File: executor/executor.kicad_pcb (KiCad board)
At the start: 2 copper layers, 0 parts

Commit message: [New] complete executor PCB layout
Signed-off-by: Homalozoa <nx.tardis@gmail.com>
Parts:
- added C1: 10uF, 20%, 50V, Capacitor_SMD:C_0805_2012Metric, F.Cu at (72.5, 69.2)
- added C10: 10uF, 10%, 50V, Capacitor_SMD:C_0402_1005Metric, B.Cu at (59.1, 67.6)
- added C11: 10uF, 20%, 50V, Capacitor_SMD:C_0805_2012Metric, F.Cu at (69.1, 83.2)
- added C12: 15pF, 5%, 50V, Capacitor_SMD:C_0402_1005Metric, B.Cu at (58.0, 69.5)
- added C13: 10uF, 20%, 50V, Capacitor_SMD:C_0805_2012Metric, F.Cu at (69.1, 81.2)
- added C14: 10uF, 20%, 50V, Capacitor_SMD:C_0805_2012Metric, F.Cu at (69.1, 79.2)
- added C15: 10uF, 20%, 50V, Capacitor_SMD:C_0805_2012Metric, F.Cu at (69.1, 77.2)
- added C16: 100nF, 10%, 50V, Capacitor_SMD:C_0402_1005Metric, B.Cu at (56.9, 67.6)
- added C17: 1uF, 10%, 50V, Capacitor_SMD:C_0402_1005Metric, F.Cu at (71.4, 45.5)
- added C18: 10uF, 20%, 50V, Capacitor_SMD:C_0805_2012Metric, F.Cu at (69.0, 75.2)
- added C19: 10uF, 20%, 50V, Capacitor_SMD:C_0805_2012Metric, F.Cu at (69.1, 73.2)
- added C2: 10uF, 20%, 50V, Capacitor_SMD:C_0805_2012Metric, F.Cu at (72.5, 71.2)
- added C20: 10uF, 20%, 50V, Capacitor_SMD:C_0805_2012Metric, F.Cu at (69.1, 71.2)
- added C21: 10uF, 20%, 50V, Capacitor_SMD:C_0805_2012Metric, F.Cu at (69.1, 69.2)
- added C22: 47uF, 10% 50V, Capacitor_SMD:CP_Elec_8x6.2, B.Cu at (70.9, 82.0)
- added C23: 100nF, 10%, 50V, Capacitor_SMD:C_0402_1005Metric, B.Cu at (67.0, 67.8)
- added C24: 100nF, 10%, 50V, Capacitor_SMD:C_0402_1005Metric, B.Cu at (70.8, 70.9)
- added C25: 1uF, 10%, 50V, Capacitor_SMD:C_0402_1005Metric, F.Cu at (79.9, 45.5)
- added C26: 4.7uF, 20%, 50V, Capacitor_SMD:C_0603_1608Metric, B.Cu at (71.1, 75.1)
- added C27: 100nF, 10%, 10V, Capacitor_SMD:C_0402_1005Metric, F.Cu at (94.2, 72.6)
- added C28: 4.7uF, 20%, 50V, Capacitor_SMD:C_0603_1608Metric, B.Cu at (72.7, 75.1)
- added C29: 1uF, 10%, 50V, Capacitor_SMD:C_0402_1005Metric, F.Cu at (87.6, 37.3)
- added C3: 10uF, 20%, 50V, Capacitor_SMD:C_0805_2012Metric, F.Cu at (72.5, 73.2)
- added C30: 100nF, 10%, 50V, Capacitor_SMD:C_0402_1005Metric, B.Cu at (72.8, 70.9)
- added C31: 4.7uF, 20%, 50V, Capacitor_SMD:C_0603_1608Metric, B.Cu at (61.6, 57.0)
- added C32: 1nF, 10%, 50V, Capacitor_SMD:C_0402_1005Metric, F.Cu at (48.1, 56.5)
- added C33: 100nF, 10%, 10V, Capacitor_SMD:C_0402_1005Metric, F.Cu at (87.6, 71.1)
- added C34: 4.7uF, 20%, 50V, Capacitor_SMD:C_0603_1608Metric, B.Cu at (61.6, 55.4)
- added C35: 1nF, 10%, 50V, Capacitor_SMD:C_0402_1005Metric, F.Cu at (48.1, 57.5)
- added C36: 100nF, 10%, 50V, Capacitor_SMD:C_0402_1005Metric, F.Cu at (48.1, 55.4)
- added C37: 1uF, 10%, 50V, Capacitor_SMD:C_0402_1005Metric, F.Cu at (54.3, 52.3)
- added C38: 10pF, 10%, 10V, Capacitor_SMD:C_0402_1005Metric, F.Cu at (82.8, 66.1)
- added C39: 100nF, 10%, 10V, Capacitor_SMD:C_0402_1005Metric, B.Cu at (87.3, 67.1)
- added C4: 10uF, 20%, 50V, Capacitor_SMD:C_0805_2012Metric, F.Cu at (72.5, 75.2)
- added C40: 10uF, 10%, 10V, Capacitor_SMD:C_0402_1005Metric, F.Cu at (86.1, 71.8)
- added C41: 100nF, 10%, 10V, Capacitor_SMD:C_0402_1005Metric, B.Cu at (96.0, 53.5)
- added C42: 10pF, 10%, 10V, Capacitor_SMD:C_0402_1005Metric, F.Cu at (86.2, 69.7)
- added C43: 100nF, 10%, 10V, Capacitor_SMD:C_0402_1005Metric, F.Cu at (85.4, 72.5)
- added C44: 100nF, 10%, 10V, Capacitor_SMD:C_0402_1005Metric, B.Cu at (93.2, 56.3)
- added C45: 10uF, 10%, 10V, Capacitor_SMD:C_0402_1005Metric, B.Cu at (88.9, 69.7)
- added C46: 100nF, 10%, 10V, Capacitor_SMD:C_0402_1005Metric, B.Cu at (89.6, 69.0)
- added C47: 4.7uF, 10%, 10V, Capacitor_SMD:C_0402_1005Metric, B.Cu at (94.6, 54.9)
- added C48: 1uF, 10%, 10V, Capacitor_SMD:C_0402_1005Metric, F.Cu at (58.9, 59.4)
- added C49: 47nF, 10%, 50V, Capacitor_SMD:C_0402_1005Metric, F.Cu at (56.2, 52.3)
- added C5: 10uF, 20%, 50V, Capacitor_SMD:C_0805_2012Metric, F.Cu at (72.5, 77.2)
- added C50: 1uF, 10%, 10V, Capacitor_SMD:C_0402_1005Metric, B.Cu at (93.9, 55.6)
- added C51: 100nF, 10%, 10V, Capacitor_SMD:C_0402_1005Metric, B.Cu at (95.3, 54.2)
- added C52: 100nF, 10%, 10V, Capacitor_SMD:C_0402_1005Metric, F.Cu at (61.0, 58.3)
- added C53: 10pF, 10%, 50V, Capacitor_SMD:C_0402_1005Metric, B.Cu at (81.0, 66.3)
- added C54: 10nF, 10%, 50V, Capacitor_SMD:C_0402_1005Metric, B.Cu at (75.4, 73.2)
- added C55: 10pF, 10%, 50V, Capacitor_SMD:C_0402_1005Metric, B.Cu at (75.9, 65.9)
- added C56: 10nF, 10%, 10V, Capacitor_SMD:C_0402_1005Metric, F.Cu at (72.1, 65.1)
- added C57: 2.2uF, 10%, 10V, Capacitor_SMD:C_0402_1005Metric, F.Cu at (72.1, 64.1)
- added C58: 100nnF, 10%, 10V, Capacitor_SMD:C_0402_1005Metric, F.Cu at (72.1, 63.1)
- added C59: 300nF, 10%, 50V, Capacitor_SMD:C_0402_1005Metric, B.Cu at (75.9, 68.2)
- added C6: 10uF, 10%, 50V, Capacitor_SMD:C_0402_1005Metric, B.Cu at (58.0, 67.6)
- added C60: 100pF, 10%, 10V, Capacitor_SMD:C_0402_1005Metric, B.Cu at (81.2, 74.9)
- added C61: 100nF, 10%, 10V, Capacitor_SMD:C_0402_1005Metric, B.Cu at (69.5, 59.4)
- added C62: 100pF, 10%, 10V, Capacitor_SMD:C_0402_1005Metric, B.Cu at (76.0, 75.5)
- added C63: 1uF, 10%, 10V, Capacitor_SMD:C_0402_1005Metric, B.Cu at (70.5, 59.4)
- added C64: 100nF, 10%, 50V, Capacitor_SMD:C_0402_1005Metric, B.Cu at (74.8, 70.9)
- added C65: 10uF, 10%, 50V, Capacitor_SMD:C_0402_1005Metric, B.Cu at (75.8, 70.9)
- added C66: 10uF, 10%, 50V, Capacitor_SMD:C_0402_1005Metric, B.Cu at (74.3, 69.5)
- added C7: 10uF, 20%, 50V, Capacitor_SMD:C_0805_2012Metric, F.Cu at (72.5, 79.2)
- added C8: 10uF, 20%, 50V, Capacitor_SMD:C_0805_2012Metric, F.Cu at (72.5, 81.2)
- added C9: 10uF, 20%, 50V, Capacitor_SMD:C_0805_2012Metric, F.Cu at (72.5, 83.2)
- added D1: 5V, Diode_SMD:D_SOD-923, B.Cu at (55.8, 67.7)
- added D2: BAV99, Package_TO_SOT_SMD:SOT-23, B.Cu at (61.5, 78.6)
- added D3: ESD56161D30, Rolling_Custom:DFN2x2-3L, B.Cu at (68.8, 74.4)
- added D4: BAV99, Package_TO_SOT_SMD:SOT-23, B.Cu at (50.1, 64.4)
- added D5: BAV99, Package_TO_SOT_SMD:SOT-23, B.Cu at (53.8, 64.4)
- added D6: BAV99, Package_TO_SOT_SMD:SOT-23, B.Cu at (57.6, 64.4)
- added D7: Blue, LED_SMD:LED_0402_1005Metric, F.Cu at (97.6, 73.3)
- added D8: 12V, Diode_SMD:D_SOD-323, B.Cu at (79.6, 75.0)
- added D9: 12V, Diode_SMD:D_SOD-323, B.Cu at (77.6, 75.0)
- added J1: XT30PW(2+2), Rolling_Custom:XT30PW(2+2), F.Cu at (83.3, 82.8)
- added L1: 10uH, Inductor_SMD:L_Coilcraft_XxL4040, B.Cu at (62.2, 68.2)
- added L2: 20R, Resistor_SMD:R_0402_1005Metric, B.Cu at (88.1, 71.2)
- added NT1: NetTie, NetTie:NetTie-2_SMD_Pad0.5mm, F.Cu at (74.0, 66.3)
- added Q1: WNM6006, Rolling_Custom:PDFN5X6-8L, F.Cu at (67.8, 39.9)
- added Q2: WNM6006, Rolling_Custom:PDFN5X6-8L, F.Cu at (67.8, 51.2)
- added Q3: WNM6006, Rolling_Custom:PDFN5X6-8L, F.Cu at (75.8, 39.9)
- added Q4: WNM6006, Rolling_Custom:PDFN5X6-8L, F.Cu at (75.8, 51.2)
- added Q5: WNM6006, Rolling_Custom:PDFN5X6-8L, F.Cu at (83.2, 39.9)
- added Q6: WNM6006, Rolling_Custom:PDFN5X6-8L, F.Cu at (83.2, 51.2)
- added R1: 0, Resistor_SMD:R_0402_1005Metric, F.Cu at (63.9, 49.2)
- added R10: 100k, 5%, Resistor_SMD:R_0402_1005Metric, B.Cu at (71.3, 72.9)
- added R11: 100k, 5%, Resistor_SMD:R_0402_1005Metric, B.Cu at (71.8, 70.9)
- added R12: 0, Resistor_SMD:R_0402_1005Metric, F.Cu at (79.7, 37.4)
- added R13: 0, Resistor_SMD:R_0402_1005Metric, F.Cu at (79.7, 48.6)
- added R14: 10k, 5%, Resistor_SMD:R_0402_1005Metric, F.Cu at (93.4, 71.8)
- added R15: 10k, 5%, Resistor_SMD:R_0402_1005Metric, F.Cu at (92.6, 71.0)
- added R16: 0.001R, Resistor_SMD:R_1206_3216Metric, F.Cu at (55.4, 46.9)
- added R17: 10k, 5%, Resistor_SMD:R_0402_1005Metric, F.Cu at (86.9, 70.4)
- added R18: 10k, 5%, Resistor_SMD:R_0402_1005Metric, B.Cu at (88.1, 67.9)
- added R19: 0, Resistor_SMD:R_0402_1005Metric, B.Cu at (87.3, 70.4)
- added R2: 0, Resistor_SMD:R_0402_1005Metric, F.Cu at (63.9, 37.4)
- added R20: 10k, 5%, Resistor_SMD:R_0402_1005Metric, F.Cu at (61.0, 59.4)
- added R21: 100R, 5%, Resistor_SMD:R_0402_1005Metric, F.Cu at (61.0, 60.5)
- added R22: 100R, 5%, Resistor_SMD:R_0402_1005Metric, F.Cu at (61.0, 61.5)
- added R23: 100R, 5%, Resistor_SMD:R_0402_1005Metric, F.Cu at (61.0, 62.5)
- added R27: 10k, 5%, Resistor_SMD:R_0402_1005Metric, F.Cu at (84.8, 59.5)
- added R28: 0R, 5%, Resistor_SMD:R_0402_1005Metric, B.Cu at (96.3, 59.1)
- added R29: 0R, 5%, Resistor_SMD:R_0402_1005Metric, B.Cu at (95.6, 58.4)
- added R3: 150k, 5%, Resistor_SMD:R_0402_1005Metric, B.Cu at (59.1, 69.5)
- added R30: 0R, 5%, Resistor_SMD:R_0402_1005Metric, B.Cu at (94.9, 57.7)
- added R31: 100R, 5%, Resistor_SMD:R_0402_1005Metric, B.Cu at (65.6, 79.8)
- added R32: 33k, Resistor_SMD:R_0402_1005Metric, B.Cu at (75.4, 74.1)
- added R33: 10k, 5%, Resistor_SMD:R_0402_1005Metric, F.Cu at (96.9, 72.6)
- added R34: 3k, Resistor_SMD:R_0402_1005Metric, B.Cu at (73.8, 70.9)
- added R36: 2.2k, 5%, Resistor_SMD:R_0402_1005Metric, F.Cu at (74.2, 57.6)
- added R37: 2.2k, 5%, Resistor_SMD:R_0402_1005Metric, F.Cu at (75.8, 57.6)
- added R38: 120R, Resistor_SMD:R_0402_1005Metric, B.Cu at (86.2, 76.2)
- added R4: 47k, 1%, Resistor_SMD:R_0402_1005Metric, B.Cu at (69.8, 70.9)
- added R5: 150k, 5%, Resistor_SMD:R_0402_1005Metric, B.Cu at (64.5, 81.8)
- added R6: 10k, 5%, Resistor_SMD:R_0402_1005Metric, B.Cu at (64.5, 79.8)
- added R7: 0, Resistor_SMD:R_0402_1005Metric, F.Cu at (72.0, 37.3)
- added R8: 0, Resistor_SMD:R_0402_1005Metric, F.Cu at (71.9, 48.6)
- added R9: 0.001R, Resistor_SMD:R_1206_3216Metric, F.Cu at (55.4, 49.2)
- added TP1: 3V3, TestPoint:TestPoint_Pad_D2.0mm, F.Cu at (50.6, 69.2)
- added TP10: C, TestPoint:TestPoint_Plated_Hole_D2.0mm, F.Cu at (83.4, 45.6)
- added TP13: NTC+, TestPoint:TestPoint_Loop_D1.80mm_Drill1.0mm_Beaded, F.Cu at (97.3, 47.2)
- added TP14: NTC-, TestPoint:TestPoint_Loop_D1.80mm_Drill1.0mm_Beaded, F.Cu at (99.7, 50.6)
- added TP4: SWDIO, TestPoint:TestPoint_Pad_D1.5mm, F.Cu at (102.1, 56.6)
- added TP5: SWCLK, TestPoint:TestPoint_Pad_D1.5mm, F.Cu at (101.0, 53.9)
- added TP7: A, TestPoint:TestPoint_Plated_Hole_D2.0mm, F.Cu at (68.0, 45.6)
- added TP8: B, TestPoint:TestPoint_Plated_Hole_D2.0mm, F.Cu at (76.0, 45.6)
- added U1: WD1601E, Package_TO_SOT_SMD:SOT-23-6, B.Cu at (67.0, 70.3)
- added U2: DRV8323SRTAT, Rolling_Custom:WQFN40, F.Cu at (54.1, 57.9)
- added U3: GD32F303RETx, Package_QFP:LQFP-64_10x10mm_P0.5mm, F.Cu at (92.0, 62.9)
- added U4: TCAN4550RGYRQ1, Rolling_Custom:VQFN20, B.Cu at (78.6, 70.5)
- added U5: AS5047P-ATSM, Package_SO:TSSOP-14_4.4x5mm_P0.65mm, B.Cu at (75.0, 60.0)
- added U6: QMA7981, Package_LGA:LGA-12_2x2mm_P0.5mm, F.Cu at (75.0, 60.0)
- added Y1: 8M, Oscillator:Oscillator_SMD_EuroQuartz_XO32-4Pin_3.2x2.5mm, F.Cu at (84.6, 67.8)
- added Y2: 40M, Oscillator:Oscillator_SMD_EuroQuartz_XO32-4Pin_3.2x2.5mm, B.Cu at (78.4, 66.2)
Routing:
- net GND: track 0.00 -> 240.9 mm, vias 0 -> 17
- net +3V3: track 0.00 -> 223.9 mm, vias 0 -> 14
- net VM: track 0.00 -> 170.9 mm, vias 0 -> 8
- net IAN: track 0.00 -> 170.4 mm, vias 0 -> 10
- net C: track 0.00 -> 77.6 mm, vias 0 -> 2
- net ICP: track 0.00 -> 69.6 mm, vias 0 -> 4
- net DRV_EN: track 0.00 -> 62.9 mm, vias 0 -> 4
- net IBP: track 0.00 -> 59.1 mm, vias 0 -> 4
- net DRV_SCK: track 0.00 -> 53.7 mm, vias 0 -> 2
- net DRV_SCS: track 0.00 -> 53.4 mm, vias 0 -> 2
- net B: track 0.00 -> 53.2 mm, vias 0 -> 3
- net DRV_SDO: track 0.00 -> 52.2 mm, vias 0 -> 2
- net DRV_SDI: track 0.00 -> 51.9 mm, vias 0 -> 2
- net ISENSE_A: track 0.00 -> 50.8 mm, vias 0 -> 2
- net PWM_A: track 0.00 -> 44.7 mm, vias 0 -> 2
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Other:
- board outline added: 58 x 58 mm
- copper layers 2 -> 4

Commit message: [New] Complete executor ver 0.1
Signed-off-by: Homalozoa <nx.tardis@gmail.com>
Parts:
- removed R16: 0.001R, Resistor_SMD:R_1206_3216Metric
- C10, C12, C16, C31, C34, C53, C54, C55, C59, C6, C60, C62, C64, C65, C66, D1, D4, D6, D8, D9, R3, R32, R34, R38, R4, R5, R6, U4, Y2: moved to F.Cu
- C17, C25, C29, C56, C57, C58, NT1, Q1, Q2, Q3, Q4, Q5, Q6, R1, R12, R13, R2, R7, R8, R9, TP10, TP7, TP8: moved to B.Cu
- moved TP14 51.8 mm to (53.9, 74.9)
- moved TP13 51.8 mm to (51.5, 71.4)
- moved TP4 50.3 mm to (53.2, 44.9), turned to 135 degrees
- moved TP5 50.2 mm to (51.4, 46.7), turned to 135 degrees
- moved Q1 41.1 mm to (97.5, 68.3), turned to 0 degrees
- moved R2 40.6 mm to (94.1, 64.6), turned to 0 degrees
- moved C11 38.6 mm to (82.2, 46.9), turned to 0 degrees
- moved D7 37.0 mm to (61.9, 82.9), turned to -135 degrees
- moved C27 36.5 mm to (58.1, 67.2)
- moved C45 35.5 mm to (53.7, 65.1)
- moved R17 35.5 mm to (51.7, 65.8)
- moved U3 35.5 mm to (56.8, 58.3)
- moved C33 35.5 mm to (52.4, 66.5)
- moved C39 35.5 mm to (52.1, 62.5)
- moved C46 35.5 mm to (54.4, 64.4)
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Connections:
- net IAN renamed GNDA
- net VM renamed +24V
- R29 pad 2: PWM_C -> PWM_B
- R30 pad 2: PWM_B -> PWM_C
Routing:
- net GND: track 240.9 -> 285.5 mm, vias 17 -> 10
- net CAN_L: track 19.1 -> 60.2 mm, vias 0 -> 2
- net A: track 44.5 -> 85.2 mm
- net ECD_MOSI: track 10.9 -> 47.5 mm, vias 1 -> 2
- net ECD_MISO: track 11.2 -> 44.6 mm, vias 1 -> 2
- net CAN_H: track 22.1 -> 54.7 mm, vias 0 -> 2
- net ICP: track 69.6 -> 37.8 mm, vias 4 -> 3
- net ECD_SCK: track 11.6 -> 41.2 mm, vias 1 -> 2
- net +24V: track 170.9 -> 200.2 mm, vias 8 -> 6
- net Net-(R31-Pad1): track 36.3 -> 7.32 mm, vias 2 -> 1
- net TCAN_SDO: track 33.0 -> 5.13 mm, vias 3 -> 0
- net TEMP_MOTOR: track 38.3 -> 10.6 mm, vias 2 -> 0
- net VGL_A: track 19.6 -> 46.4 mm
- net TCAN_SDI: track 31.8 -> 5.01 mm, vias 3 -> 2
- net VGH_A: track 21.8 -> 48.5 mm, vias 2 -> 3
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- added copper zone on In2.Cu, net +24V
- added copper zone on In1.Cu, net +3V3
- added copper zone on B.Cu, net GND
- added copper zone on F.Cu, net GND
- added copper zone on B.Cu, net GNDA
- added copper zone on F.Cu, net GNDA

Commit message: [New] Add prj cerebellum & limbic_cm4 & limbic_x3m
Signed-off-by: Homalozoa <nx.tardis@gmail.com>
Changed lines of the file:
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@@
   (gr_arc locked (start 98.276504 42.702475) (mid 103.997113 60) (end 98.276504 77.297525) (layer "Edge.Cuts") (width 0.15))
   (gr_arc locked (start 57.702475 83.276504) (mid 56.895935 81.638704) (end 57.755316 80.028002) (layer "Edge.Cuts") (width 0.15))
-  (gr_arc locked (start 51.723495 42.702475) (mid 53.361295 41.895935) (end 54.971998 42.755316) (layer "Edge.Cuts") (width 0.15))
+  (gr_arc locked (start 51.723495 42.702475) (mid 53.361295 41.895936) (end 54.971998 42.755316) (layer "Edge.Cuts") (width 0.15))
   (gr_arc locked (start 92.297526 83.276504) (mid 75.000001 88.997113) (end 57.702475 83.276504) (layer "Edge.Cuts") (width 0.15))
   (gr_arc locked (start 57.702474 36.723496) (mid 75 31.002886) (end 92.297525 36.723496) (layer "Edge.Cuts") (width 0.15))
@@
   (segment (start 86 56.485) (end 86 48.085) (width 0.254) (layer "In1.Cu") (net 37))
   (segment (start 86.4 56.885) (end 86 56.485) (width 0.254) (layer "In1.Cu") (net 37))
-  (segment (start 67.952957 37.288589) (end 74.584109 37.288589) (width 0.254) (layer "In2.Cu") (net 37))
   (segment (start 67.4 37.841546) (end 67.952957 37.288589) (width 0.254) (layer "In2.Cu") (net 37))
   (segment (start 85.38052 48.085) (end 86 48.085) (width 0.254) (layer "In2.Cu") (net 37))
   (segment (start 74.584109 37.288589) (end 85.38052 48.085) (width 0.254) (layer "In2.Cu") (net 37))
   (segment (start 67.4 38.885) (end 67.4 37.841546) (width 0.254) (layer "In2.Cu") (net 37))
+  (segment (start 67.952957 37.288589) (end 74.584109 37.288589) (width 0.254) (layer "In2.Cu") (net 37))
   (segment (start 89.536048 62.428) (end 91.779048 60.185) (width 0.762) (layer "B.Cu") (net 37))
   (segment (start 94.598048 59.888) (end 92.076048 59.888) (width 0.762) (layer "B.Cu") (net 37))
@@
     )
   )
-  (zone (net 0) (net_name "") (layers "F.Cu" "In1.Cu" "In2.Cu") (hatch edge 0.508)
+  (zone (net 0) (net_name "") (layers "F.Cu" "In1.Cu" "In2.Cu" "B.Cu") (hatch edge 0.508)
     (connect_pads (clearance 0))
     (min_thickness 0.254)

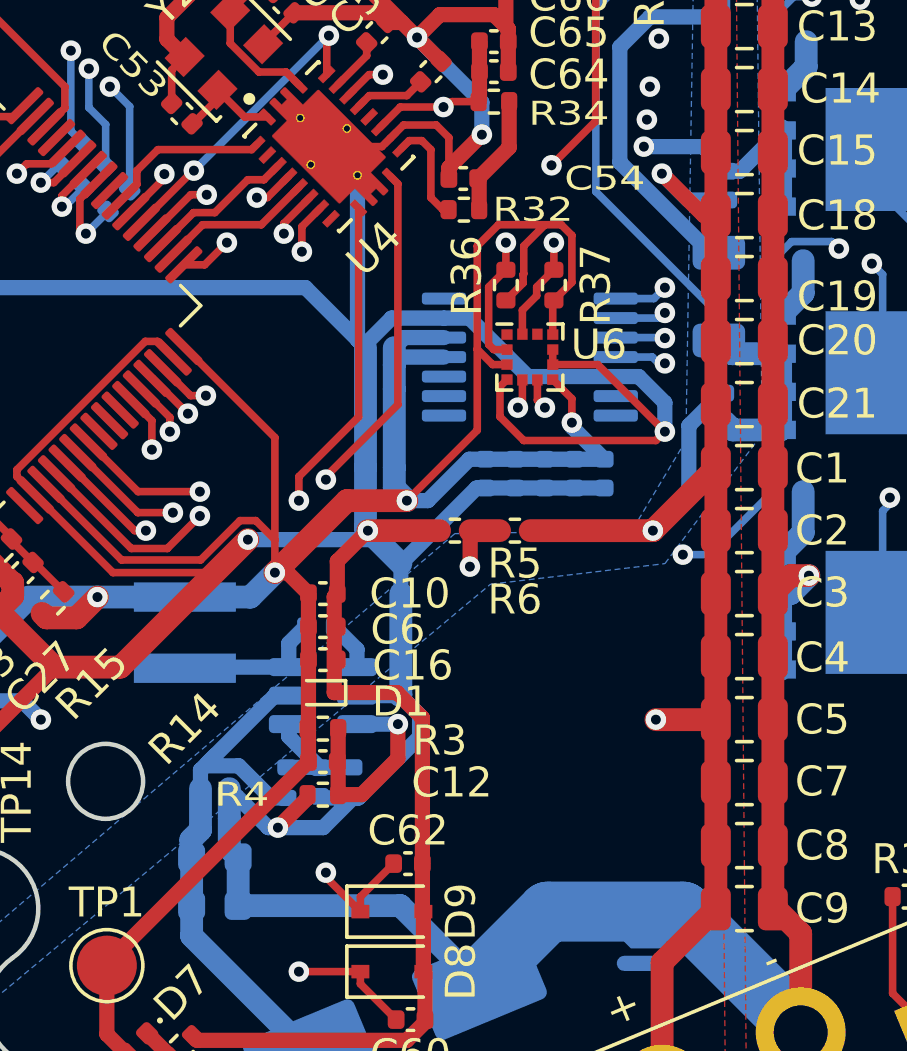
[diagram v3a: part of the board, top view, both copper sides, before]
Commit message: [Fix] Move Acc sensor to avoid mechanical stress
Signed-off-by: Homalozoa <nx.tardis@gmail.com>
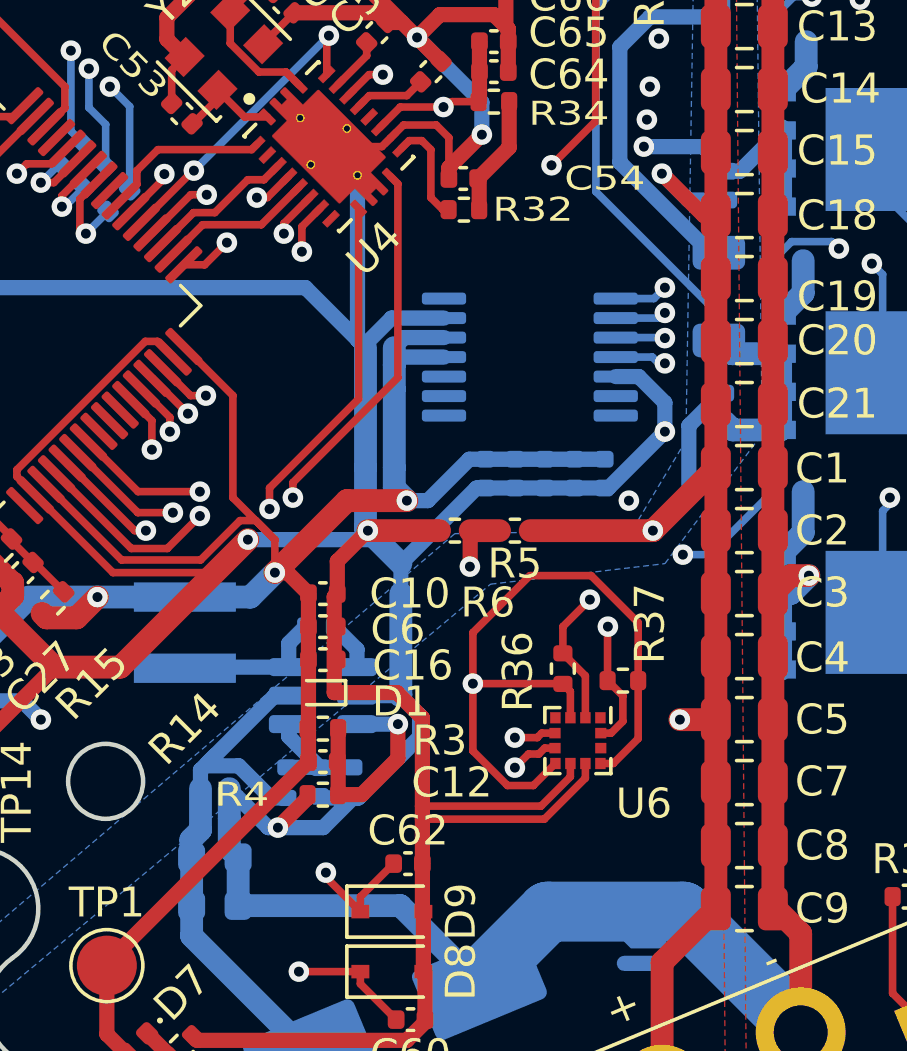
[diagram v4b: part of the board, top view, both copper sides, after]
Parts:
- moved R37 13.4 mm to (78.1, 70.8), turned to 0 degrees
- moved R36 12.9 mm to (76.1, 70.4)
- moved U6 12.9 mm to (76.6, 72.8), turned to -90 degrees
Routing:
- net +3V3: track 208.5 -> 216.0 mm, vias 11 -> 12
- net ACC_INT1: track 14.7 -> 21.5 mm
- net ACC_INT2: track 16.7 -> 22.7 mm
- net GND: track 285.5 -> 281.6 mm
- net ACC_SDA: track 18.3 -> 22.1 mm
- net ACC_SCL: track 19.7 -> 22.9 mm
- net +24V: track 200.2 -> 198.6 mm
- net CAN_H: track 54.7 -> 55.6 mm
- net CAN_L: track 60.2 -> 61.0 mm
